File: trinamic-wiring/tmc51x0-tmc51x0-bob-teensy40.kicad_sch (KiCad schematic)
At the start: 4 parts, among them M1 Stepper_Motor

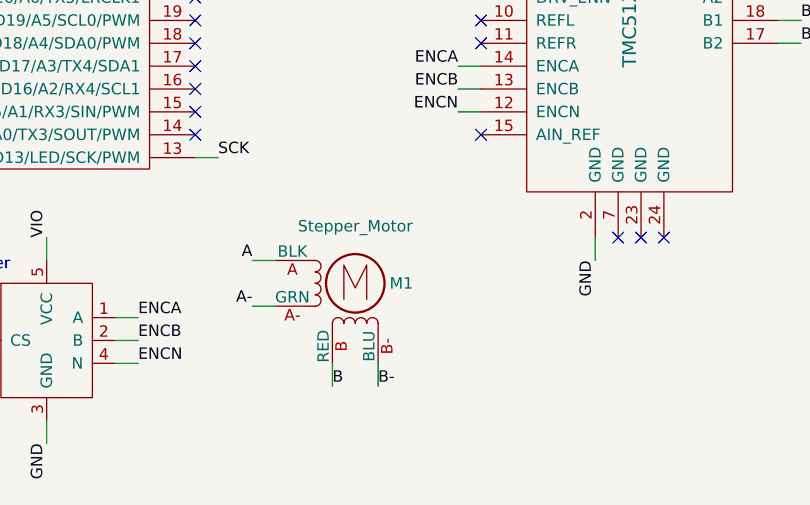
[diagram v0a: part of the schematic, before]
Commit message: Split tmc51x0 into spi and uart
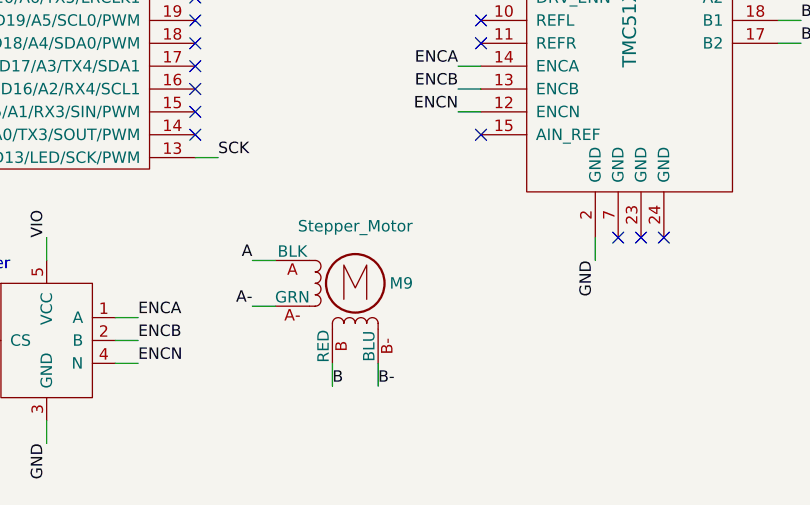
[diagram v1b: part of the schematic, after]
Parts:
- renumbered A1 to A4, ENC2 to ENC1, M1 to M9
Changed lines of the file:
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@@
   (title_block
     (title "Trinamic Wiring")
-    (date "2024-07-31")
+    (date "2024-08-01")
     (rev "0.5")
     (company "Janelia Research Campus")
@@
   (symbol (lib_id "Janelia:TEENSY_4.0_HEADERS") (at 100.33 102.87 0) (unit 1)
     (in_bom yes) (on_board yes) (dnp no) (fields_autoplaced)
-    (property "Reference" "A1" (at 100.33 83.82 0) (do_not_autoplace)
+    (property "Reference" "A4" (at 100.33 83.82 0) (do_not_autoplace)
       (effects (font (size 1.524 1.524)) hide)
     )
@@
     (instances
       (project "trinamic-wiring"
-        (path "/e4144788-6304-493f-818e-5d881d3b7418/a161638e-a96f-4455-865a-1d7502675f43/176cb0b5-cab1-47ac-9998-e59b71e39393/106cbaaa-dd32-4d4d-a442-e3c42a8253b0"
-          (reference "A1") (unit 1)
+        (path "/e4144788-6304-493f-818e-5d881d3b7418/a161638e-a96f-4455-865a-1d7502675f43/ca35872a-a0db-401c-97bd-5b4a3f731cf1/abe2ac4d-e9f3-44e3-a772-2451bb376256/106cbaaa-dd32-4d4d-a442-e3c42a8253b0"
+          (reference "A4") (unit 1)
         )
       )
@@
   (symbol (lib_id "Janelia:ENCODER_EMS22Q") (at 115.57 139.7 0) (unit 1)
     (in_bom yes) (on_board yes) (dnp no) (fields_autoplaced)
-    (property "Reference" "ENC2" (at 118.11 132.08 0)
+    (property "Reference" "ENC1" (at 118.11 132.08 0)
       (effects (font (size 1.524 1.524)) hide)
     )
@@
     (instances
       (project "trinamic-wiring"
-        (path "/e4144788-6304-493f-818e-5d881d3b7418/a161638e-a96f-4455-865a-1d7502675f43/176cb0b5-cab1-47ac-9998-e59b71e39393/106cbaaa-dd32-4d4d-a442-e3c42a8253b0"
-          (reference "ENC2") (unit 1)
+        (path "/e4144788-6304-493f-818e-5d881d3b7418/a161638e-a96f-4455-865a-1d7502675f43/ca35872a-a0db-401c-97bd-5b4a3f731cf1/abe2ac4d-e9f3-44e3-a772-2451bb376256/106cbaaa-dd32-4d4d-a442-e3c42a8253b0"
+          (reference "ENC1") (unit 1)
         )
       )
@@
     (instances
       (project "trinamic-wiring"
-        (path "/e4144788-6304-493f-818e-5d881d3b7418/a161638e-a96f-4455-865a-1d7502675f43/176cb0b5-cab1-47ac-9998-e59b71e39393/106cbaaa-dd32-4d4d-a442-e3c42a8253b0"
+        (path "/e4144788-6304-493f-818e-5d881d3b7418/a161638e-a96f-4455-865a-1d7502675f43/ca35872a-a0db-401c-97bd-5b4a3f731cf1/abe2ac4d-e9f3-44e3-a772-2451bb376256/106cbaaa-dd32-4d4d-a442-e3c42a8253b0"
           (reference "BOB1") (unit 1)
         )
@@
   (symbol (lib_id "Janelia:Stepper_Motor_QSH2818-32-07-006") (at 149.86 133.35 0) (unit 1)
     (in_bom yes) (on_board yes) (dnp no)
-    (property "Reference" "M1" (at 153.67 133.35 0)
+    (property "Reference" "M9" (at 153.67 133.35 0)
       (effects (font (size 1.27 1.27)) (justify left))
     )
@@
     (instances
       (project "trinamic-wiring"
-        (path "/e4144788-6304-493f-818e-5d881d3b7418/a161638e-a96f-4455-865a-1d7502675f43/176cb0b5-cab1-47ac-9998-e59b71e39393/106cbaaa-dd32-4d4d-a442-e3c42a8253b0"
-          (reference "M1") (unit 1)
+        (path "/e4144788-6304-493f-818e-5d881d3b7418/a161638e-a96f-4455-865a-1d7502675f43/ca35872a-a0db-401c-97bd-5b4a3f731cf1/abe2ac4d-e9f3-44e3-a772-2451bb376256/106cbaaa-dd32-4d4d-a442-e3c42a8253b0"
+          (reference "M9") (unit 1)
         )
       )
